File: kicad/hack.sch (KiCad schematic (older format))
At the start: 34 parts, among them P1 USB_micro, P2 CONN_01X13, P3 CONN_01X13, P4 CONN_01X01, U1 MIC5528, U2 STF202, U3 ATSAMD21E, X1 ABS07

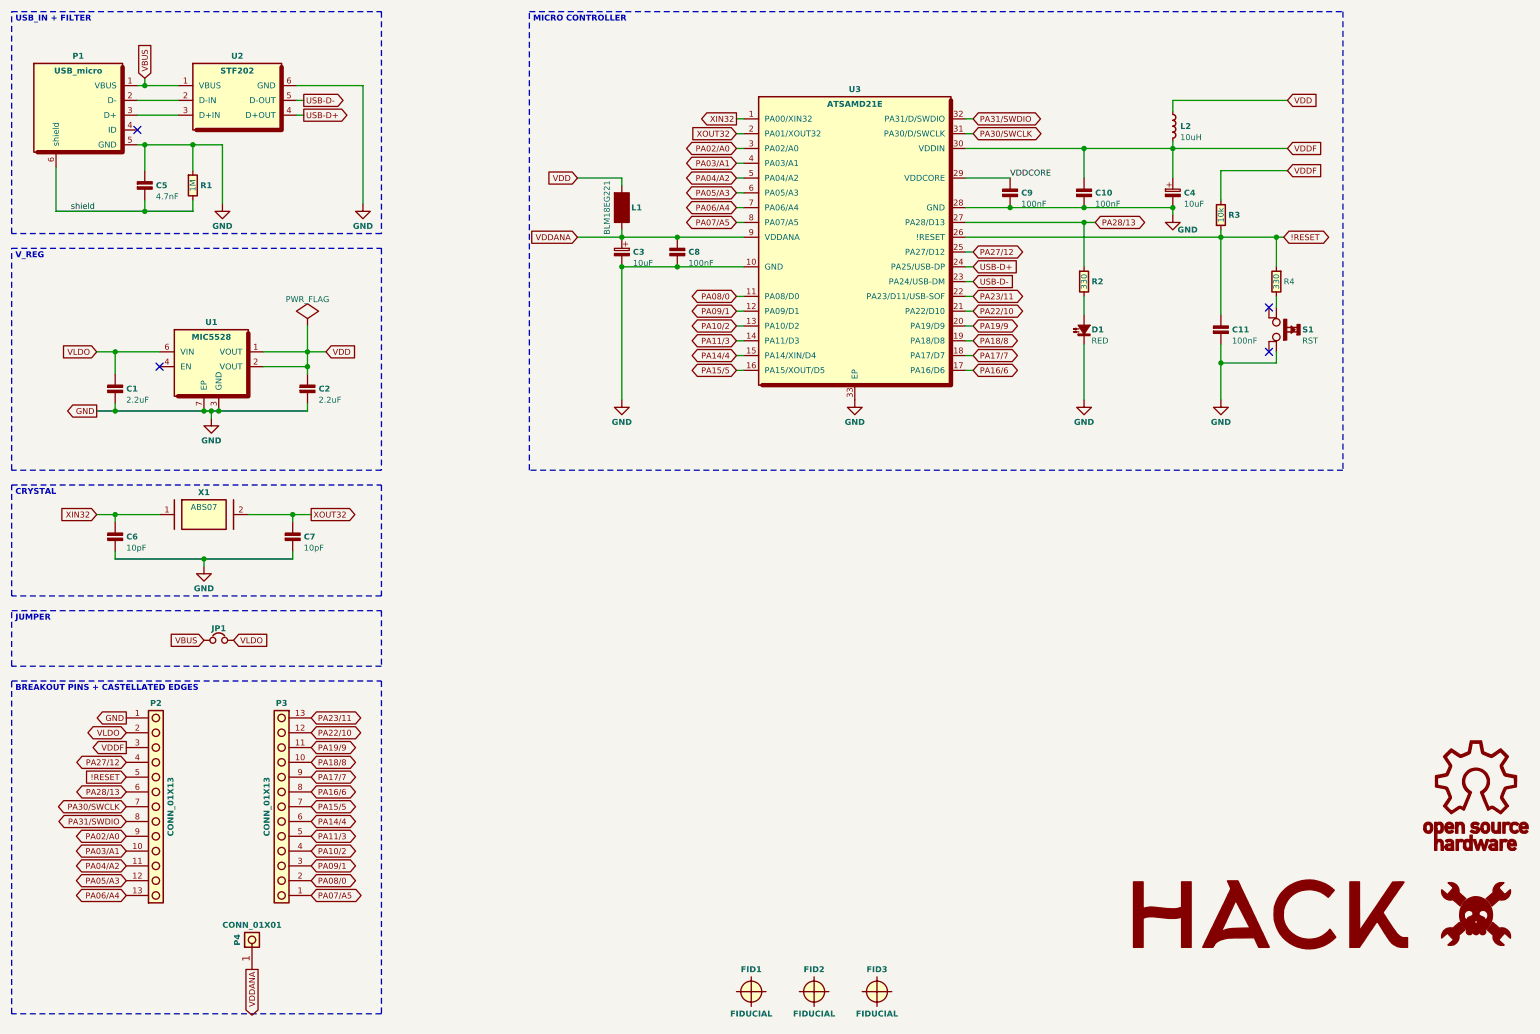
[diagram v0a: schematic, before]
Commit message: added 3d model for ELL-VFG and some other minor edits
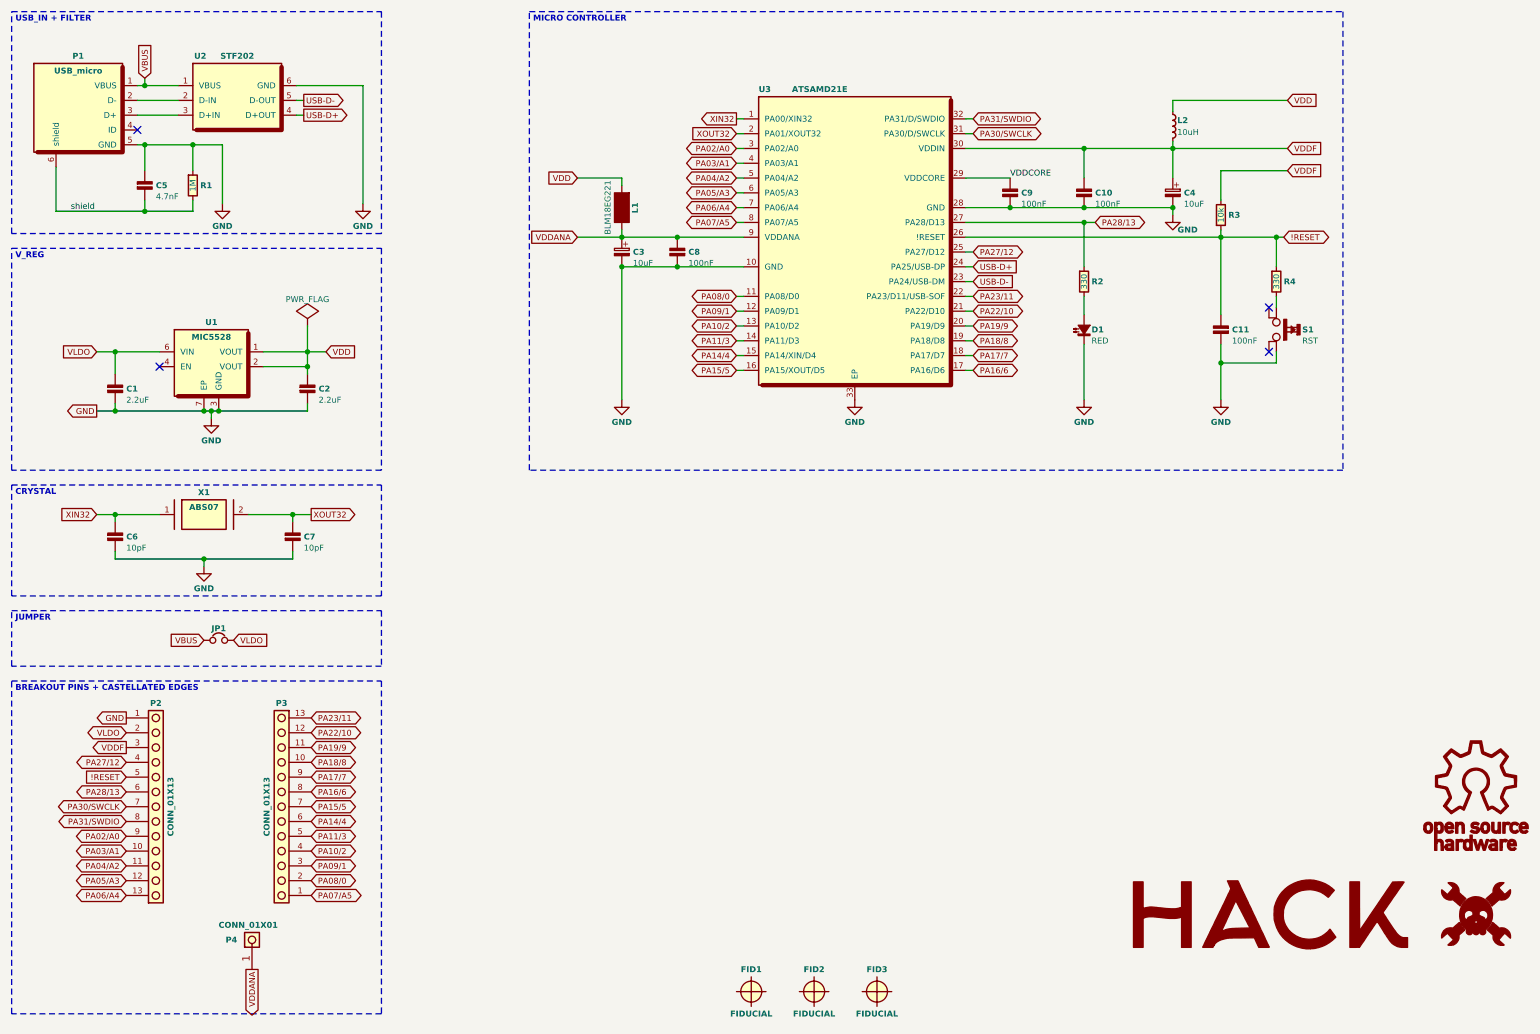
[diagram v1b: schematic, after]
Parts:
- C1, C5, C6, C8: footprint hack:C_0603_HandSoldering -> hack-footprints:C_0603_HandSoldering
- C10, C11, C9: footprint hack:C_0603_HandSoldering -> hack-footprints:C_0603_HandSoldering; manf# (none) -> 302010138
- C2: footprint hack:C_0603_HandSoldering -> hack-footprints:C_0603_HandSoldering; manf# (none) -> 302010054
- C3: footprint hack:c_elec_3x5.3 -> hack-footprints:c_elec_3x5.3
- C4: footprint hack:c_elec_3x5.3 -> hack-footprints:c_elec_3x5.3; manf# (none) -> UWX1C100MCL2GB
- C7: footprint hack:C_0603_HandSoldering -> hack-footprints:C_0603_HandSoldering; manf# (none) -> 302010097
- D1: footprint hack:LED_0603_HandSoldering -> hack-footprints:LED_0603_HandSoldering
- FID1, FID2, FID3: footprint hack:FIDUCIAL -> hack-footprints:FIDUCIAL
- JP1: footprint hack:SMD_Jumper -> hack-footprints:SMD_Jumper
- L1: footprint hack:L_0603_HandSoldering -> hack-footprints:L_0603_HandSoldering; manf# (none) -> BLM18EG221SN1D
- L2: footprint hack:ELLVFG -> hack-footprints:ELLVFG; manf# (none) -> ELL-VFG100MC
- LOGO1: footprint hack:OSHW-LOGO -> hack-footprints:OSHW-LOGO
- LOGO2: footprint hack:HACKADAY-LOGO -> hack-footprints:HACKADAY-LOGO
- LOGO3: footprint (none) -> hack-footprints:HACK-LOGO
- P1: footprint hack:47346-0001 -> hack-footprints:ST-USB-001G; manf# (none) -> 320010000
- P3: manf# (none) -> 320020128
- R1, R2, R3: footprint hack:R_0603_HandSoldering -> hack-footprints:R_0603_HandSoldering
- R4: footprint hack:R_0603_HandSoldering -> hack-footprints:R_0603_HandSoldering; manf# (none) -> 301010300
- U1: footprint hack:DFN-6-1EP_1.2x1.2mm_Pitch0.4mm -> hack-footprints:DFN-6-1EP_1.2x1.2mm_Pitch0.4mm; manf# (none) -> MIC5528-3.3YMT-TR
- U2: footprint hack:TSOP-6 -> hack-footprints:TSOP-6; manf# (none) -> STF202-22T1G
- U3: footprint hack:QFN-32-1EP_5x5mm_Pitch0.5mm -> hack-footprints:QFN-32-1EP_5x5mm_Pitch0.5mm; manf# (none) -> ATSAMD21E18A-MU
- X1: footprint (none) -> hack-footprints:xtal_3.2x1.5mm; manf# (none) -> 306010055

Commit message: Added Seeedstudio costs for some components in schematic, changed 2.2uF manf# field to real manufacturer number instead of Seeedstudio SKU
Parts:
- C1, C2: Mfr. Part # (none) -> 0; manf# 302010054 -> CC0603MRX5R5BB225
- C10, C11, C8, C9: Mfr. Part # (none) -> 0; kicost:Seeedstudio:pricing (none) -> 100:$2
- C5, C6, C7, R1, R2, R3, R4: Mfr. Part # (none) -> 0; kicost:Seeedstudio:pricing (none) -> 100:$1
- P1: Mfr. Part # (none) -> 0; kicost:Seeedstudio:pricing (none) -> 10:$3
- P2, P3: Mfr. Part # (none) -> 0; kicost:Seeedstudio:pricing (none) -> 30:$2.4
- S1: Mfr. Part # (none) -> 0; kicost:Seeedstudio:pricing (none) -> 10:$2.036
- X1: Mfr. Part # (none) -> 0; kicost:Seeedstudio:pricing (none) -> 5:$1.75
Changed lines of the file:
@@
 LIBS:power
 LIBS:hack
+LIBS:hack-cache
 EELAYER 25 0
 EELAYER END
@@
 F 2 "hack-footprints:R_0603_HandSoldering" H 2025 1975 40  0001 C CNB
 F 3 "https://github.com/MickMad/HACK/tree/master/kicad/datasheets/301010151.pdf" H 2025 1975 40  0001 C CNB
-F 4 "301010151" H 2025 1975 60  0001 C CNN "manf#"
+F 4 "0" H 2025 1975 60  0001 C CNN "Mfr. Part #"
+F 5 "301010151" H 2025 1975 60  0001 C CNN "manf#"
+F 6 "100:$1" H 2025 1975 60  0001 C CNN "kicost:Seeedstudio:pricing"
 	1    2025 1975
 	1    0    0    -1
@@
 F 2 "hack-footprints:C_0603_HandSoldering" H 1700 1975 40  0001 C CNB
 F 3 "https://github.com/MickMad/HACK/tree/master/kicad/datasheets/0100850P1.pdf" H 1700 1975 40  0001 C CNB
-F 4 "302010144" H 1700 1975 60  0001 C CNN "manf#"
+F 4 "0" H 1700 1975 60  0001 C CNN "Mfr. Part #"
+F 5 "302010144" H 1700 1975 60  0001 C CNN "manf#"
+F 6 "100:$1" H 1700 1975 60  0001 C CNN "kicost:Seeedstudio:pricing"
 	1    1700 1975
 	1    0    0    -1
@@
 F 2 "hack-footprints:C_0603_HandSoldering" H 1500 4350 40  0001 C CNB
 F 3 "https://github.com/MickMad/HACK/tree/master/kicad/datasheets/302010097.pdf" H 1500 4350 40  0001 C CNB
-F 4 "302010097" H 1500 4350 60  0001 C CNN "manf#"
+F 4 "0" H 1500 4350 60  0001 C CNN "Mfr. Part #"
+F 5 "302010097" H 1500 4350 60  0001 C CNN "manf#"
+F 6 "100:$1" H 1500 4350 60  0001 C CNN "kicost:Seeedstudio:pricing"
 	1    1500 4350
 	1    0    0    -1
@@
 F 2 "hack-footprints:C_0603_HandSoldering" H 5300 2425 40  0001 C CNB
 F 3 "https://github.com/MickMad/HACK/tree/master/kicad/datasheets/0100020P1.pdf" H 5300 2425 40  0001 C CNB
-F 4 "302010138" H 5300 2425 60  0001 C CNN "manf#"
+F 4 "0" H 5300 2425 60  0001 C CNN "Mfr. Part #"
+F 5 "302010138" H 5300 2425 60  0001 C CNN "manf#"
+F 6 "100:$2" H 5300 2425 60  0001 C CNN "kicost:Seeedstudio:pricing"
 	1    5300 2425
 	-1   0    0    -1
@@
 F 2 "hack-footprints:Pin_Castellated_1x13" H 1775 6175 40  0001 C CNB
 F 3 "https://github.com/MickMad/HACK/tree/master/kicad/datasheets/320020128.pdf" H 1775 6175 40  0001 C CNB
-F 4 "320020128" H 1775 6175 60  0001 C CNN "manf#"
+F 4 "0" H 1775 6175 60  0001 C CNN "Mfr. Part #"
+F 5 "320020128" H 1775 6175 60  0001 C CNN "manf#"
+F 6 "30:$2.4" H 1775 6175 60  0001 C CNN "kicost:Seeedstudio:pricing"
 	1    1775 6175
 	1    0    0    -1
@@
 F 2 "hack-footprints:R_0603_HandSoldering" H 8050 2625 40  0001 C CNB
 F 3 "https://github.com/MickMad/HACK/tree/master/kicad/datasheets/0011330P1.pdf" H 8050 2625 40  0001 C CNB
-F 4 "301010300" H 8050 2625 60  0001 C CNN "manf#"
+F 4 "0" H 8050 2625 60  0001 C CNN "Mfr. Part #"
+F 5 "301010300" H 8050 2625 60  0001 C CNN "manf#"
+F 6 "100:$1" H 8050 2625 60  0001 C CNN "kicost:Seeedstudio:pricing"
 	1    8050 2625
 	1    0    0    -1
@@
 F 2 "hack-footprints:SPST-PTS_810" H 9350 2950 40  0001 C CNB
 F 3 "https://github.com/MickMad/HACK/tree/master/kicad/datasheets/311020045.pdf" H 9350 2950 40  0001 C CNB
-F 4 "311020045" V 9350 2950 60  0001 C CNN "manf#"
+F 4 "0" H 9350 2950 60  0001 C CNN "Mfr. Part #"
+F 5 "311020045" V 9350 2950 60  0001 C CNN "manf#"
+F 6 "10:$2.036" V 9350 2950 60  0001 C CNN "kicost:Seeedstudio:pricing"
 	1    9350 2950
 	0    1    -1   0
@@
 F 2 "hack-footprints:R_0603_HandSoldering" H 8975 2175 40  0001 C CNB
 F 3 "https://github.com/MickMad/HACK/tree/master/kicad/datasheets/0011240P1.pdf" H 8975 2175 40  0001 C CNB
-F 4 "301010299" H 8975 2175 60  0001 C CNN "manf#"
+F 4 "0" H 8975 2175 60  0001 C CNN "Mfr. Part #"
+F 5 "301010299" H 8975 2175 60  0001 C CNN "manf#"
+F 6 "100:$1" H 8975 2175 60  0001 C CNN "kicost:Seeedstudio:pricing"
 	1    8975 2175
 	1    0    0    1
@@
 F 1 "2.2uF" H 1575 3275 40  0000 L CNN
 F 2 "hack-footprints:C_0603_HandSoldering" H 1500 3350 40  0001 C CNB
-F 3 "https://github.com/MickMad/HACK/tree/master/kicad/datasheets/302010054.pdf" H 1500 3350 40  0001 C CNB
-F 4 "302010054" H 1500 3350 60  0001 C CNN "manf#"
+F 3 "https://github.com/MickMad/HACK/tree/master/kicad/datasheets/UPY-GPHC_X5R_4V-to-50V_14_0717-202131.pdf" H 1500 3350 40  0001 C CNB
+F 4 "0" H 1500 3350 60  0001 C CNN "Mfr. Part #"
+F 5 "CC0603MRX5R5BB225" H 1500 3350 60  0001 C CNN "manf#"
 	1    1500 3350
 	1    0    0    -1
@@
 F 2 "hack-footprints:ST-USB-001G" H 1250 1150 60  0001 C CNN
 F 3 "https://github.com/MickMad/HACK/tree/master/kicad/datasheets/320010000.pdf" H 1250 1200 60  0001 C CNN
-F 4 "320010000" H 1350 1300 60  0001 C CNN "manf#"
+F 4 "0" H 1250 1150 60  0001 C CNN "Mfr. Part #"
+F 5 "320010000" H 1350 1300 60  0001 C CNN "manf#"
+F 6 "10:$3" H 1250 1150 60  0001 C CNN "kicost:Seeedstudio:pricing"
 	1    1250 1150
 	1    0    0    -1
@@
 F 1 "2.2uF" H 2875 3275 40  0000 L CNN
 F 2 "hack-footprints:C_0603_HandSoldering" H 2800 3350 40  0001 C CNB
-F 3 "https://github.com/MickMad/HACK/tree/master/kicad/datasheets/302010054.pdf" H 2800 3350 40  0001 C CNB
-F 4 "302010054" H 2800 3350 60  0001 C CNN "manf#"
+F 3 "https://github.com/MickMad/HACK/tree/master/kicad/datasheets/UPY-GPHC_X5R_4V-to-50V_14_0717-202131.pdf" H 2800 3350 40  0001 C CNB
+F 4 "0" H 2800 3350 60  0001 C CNN "Mfr. Part #"
+F 5 "CC0603MRX5R5BB225" H 2800 3350 60  0001 C CNN "manf#"
 	1    2800 3350
 	1    0    0    -1
@@
 F 2 "hack-footprints:C_0603_HandSoldering" H 2700 4350 40  0001 C CNB
 F 3 "https://github.com/MickMad/HACK/tree/master/kicad/datasheets/302010097.pdf" H 2700 4350 40  0001 C CNB
-F 4 "302010097" H 2700 4350 60  0001 C CNN "manf#"
+F 4 "0" H 2700 4350 60  0001 C CNN "Mfr. Part #"
+F 5 "302010097" H 2700 4350 60  0001 C CNN "manf#"
+F 6 "100:$1" H 2700 4350 60  0001 C CNN "kicost:Seeedstudio:pricing"
 	1    2700 4350
 	1    0    0    -1
@@
 F 2 "hack-footprints:xtal_3.2x1.5mm" H 2100 4050 60  0001 C CNN
 F 3 "https://github.com/MickMad/HACK/tree/master/kicad/datasheets/306010055.pdf" H 2100 3900 60  0001 C CNN
-F 4 "306010055" H 2200 4000 60  0001 C CNN "manf#"
+F 4 "0" H 2100 4050 60  0001 C CNN "Mfr. Part #"
+F 5 "306010055" H 2200 4000 60  0001 C CNN "manf#"
+F 6 "5:$1.75" H 2100 4050 60  0001 C CNN "kicost:Seeedstudio:pricing"
 	1    2100 4050
 	1    0    0    -1
@@
 F 2 "hack-footprints:Pin_Castellated_1x13" H 2625 6175 40  0001 C CNB
 F 3 "https://github.com/MickMad/HACK/tree/master/kicad/datasheets/320020128.pdf" H 2625 6175 40  0001 C CNB
-F 4 "320020128" H 2625 6175 60  0001 C CNN "manf#"
+F 4 "0" H 2625 6175 60  0001 C CNN "Mfr. Part #"
+F 5 "320020128" H 2625 6175 60  0001 C CNN "manf#"
+F 6 "30:$2.4" H 2625 6175 60  0001 C CNN "kicost:Seeedstudio:pricing"
 	1    2625 6175
 	-1   0    0    1
@@
 F 2 "hack-footprints:R_0603_HandSoldering" H 9350 2625 40  0001 C CNB
 F 3 "https://github.com/MickMad/HACK/tree/master/kicad/datasheets/0011330P1.pdf" H 9350 2625 40  0001 C CNB
-F 4 "301010300" H 9350 2625 60  0001 C CNN "manf#"
+F 4 "0" H 9350 2625 60  0001 C CNN "Mfr. Part #"
+F 5 "301010300" H 9350 2625 60  0001 C CNN "manf#"
+F 6 "100:$1" H 9350 2625 60  0001 C CNN "kicost:Seeedstudio:pricing"
 	1    9350 2625
 	1    0    0    -1
@@
 F 2 "hack-footprints:C_0603_HandSoldering" H 7550 2025 40  0001 C CNB
 F 3 "https://github.com/MickMad/HACK/tree/master/kicad/datasheets/0100020P1.pdf" H 7550 2025 40  0001 C CNB
-F 4 "302010138" H 7550 2025 60  0001 C CNN "manf#"
+F 4 "0" H 7550 2025 60  0001 C CNN "Mfr. Part #"
+F 5 "302010138" H 7550 2025 60  0001 C CNN "manf#"
+F 6 "100:$2" H 7550 2025 60  0001 C CNN "kicost:Seeedstudio:pricing"
 	1    7550 2025
 	-1   0    0    -1
@@
 F 2 "hack-footprints:C_0603_HandSoldering" H 8050 2025 40  0001 C CNB
 F 3 "https://github.com/MickMad/HACK/tree/master/kicad/datasheets/0100020P1.pdf" H 8050 2025 40  0001 C CNB
-F 4 "302010138" H 8050 2025 60  0001 C CNN "manf#"
+F 4 "0" H 8050 2025 60  0001 C CNN "Mfr. Part #"
+F 5 "302010138" H 8050 2025 60  0001 C CNN "manf#"
+F 6 "100:$2" H 8050 2025 60  0001 C CNN "kicost:Seeedstudio:pricing"
 	1    8050 2025
 	-1   0    0    -1
@@
 F 2 "hack-footprints:C_0603_HandSoldering" H 8975 2950 40  0001 C CNB
 F 3 "https://github.com/MickMad/HACK/tree/master/kicad/datasheets/0100020P1.pdf" H 8975 2950 40  0001 C CNB
-F 4 "302010138" H 8975 2950 60  0001 C CNN "manf#"
+F 4 "0" H 8975 2950 60  0001 C CNN "Mfr. Part #"
+F 5 "302010138" H 8975 2950 60  0001 C CNN "manf#"
+F 6 "100:$2" H 8975 2950 60  0001 C CNN "kicost:Seeedstudio:pricing"
 	1    8975 2950
 	-1   0    0    -1
